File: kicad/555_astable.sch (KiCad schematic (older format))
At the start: 10 parts, among them U2 555

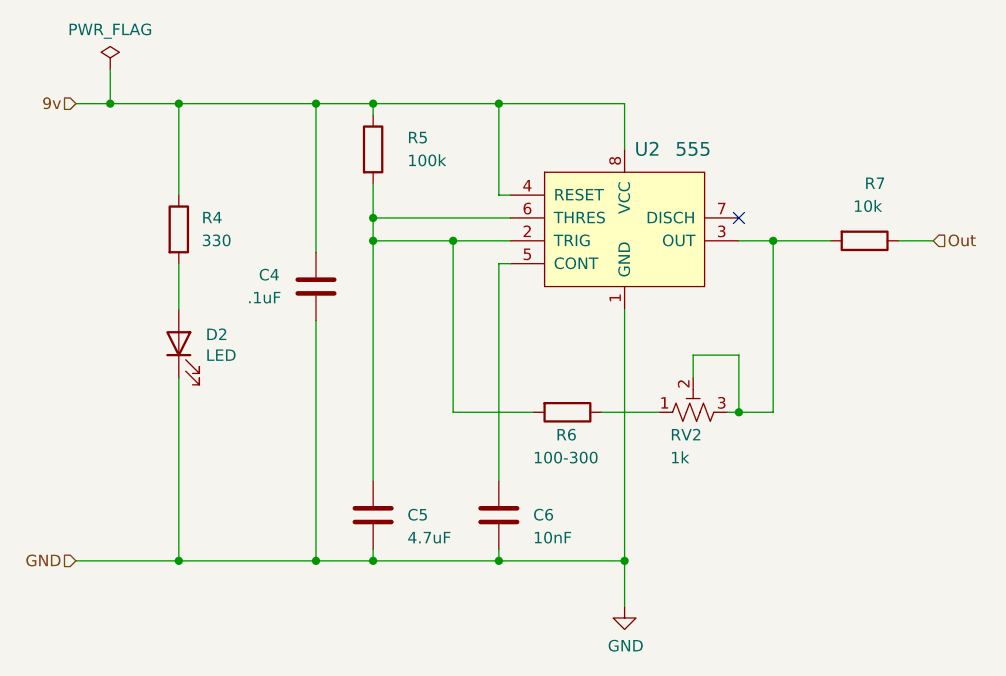
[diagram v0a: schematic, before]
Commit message: PCB revisions:
* Add voltage regulator to POLY_555
* Ditch hitch
* Reorder switches+circuits left to right
* Carve out room for battery
* Mark # 555s
* Label wired pins better

APC updates:

* Fix ground error
* Reverse volume pot direction
* Swap timing cap footprint
* Add stress relief hole for battery wires
* Widen speaker pins
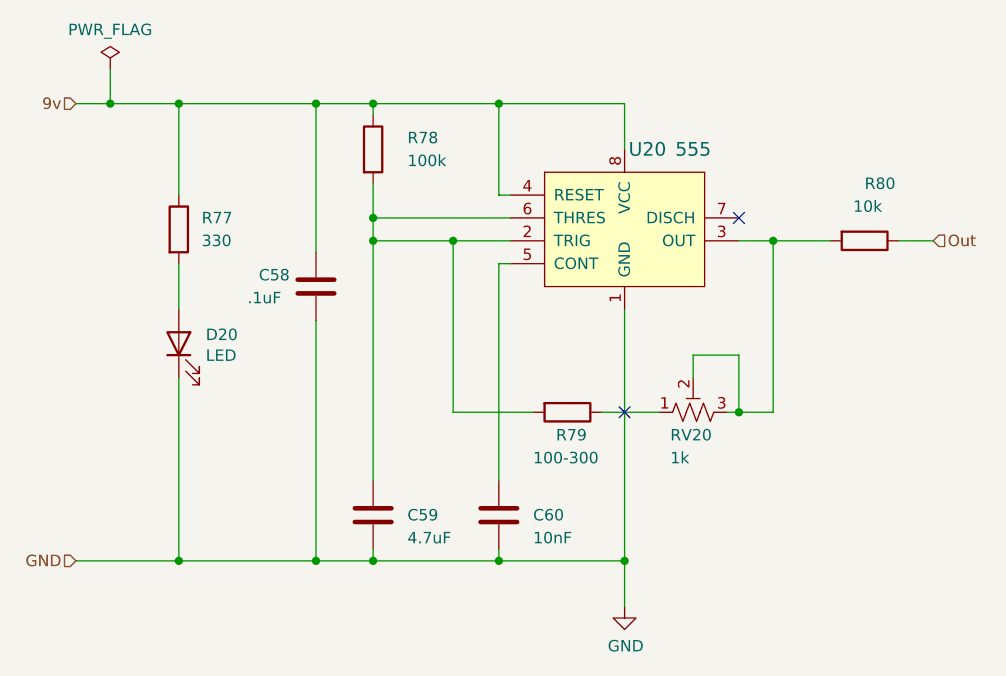
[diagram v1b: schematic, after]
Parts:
- renumbered C4 to C1, C5 to C2, C6 to C3, D2 to D1, R4 to R1, R5 to R2, R6 to R3, R7 to R4, RV2 to RV1, U2 to U1
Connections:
- no-connect marks 1 -> 2

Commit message: Update PCB
* Fix and expand battery cavity
* Fix S13-S20,C61,U21 label placements
* Fix uneven breakaway wall near APC
* Swap misplaced C62,R83 labels
* Assign C103 value
* Swap 4.7uF cap footprints and re-route
* Move LED
* Upgrade APC pots
* Move to 0,0
* Expand battery cavity even more
* Update branding: ditch _ and space, add rev, add to back side too
* Add APC rev too
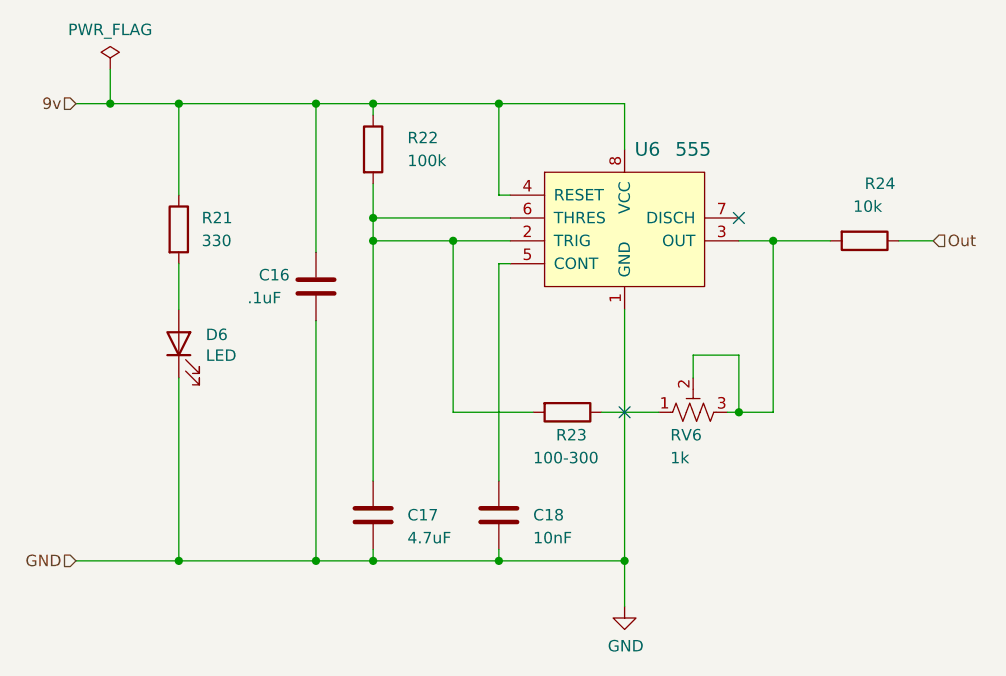
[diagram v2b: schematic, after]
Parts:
- C2: footprint Capacitor_THT:CP_Radial_D4.0mm_P2.00mm -> Capacitor_THT:CP_Radial_D5.0mm_P2.00mm
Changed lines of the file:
@@
 $Descr A4 11693 8268
 encoding utf-8
-Sheet 21 22
+Sheet 7 22
 Title ""
 Date ""
@@
 AR Path="/5F842C45/60F6A68E" Ref="R74"  Part="1"
 AR Path="/5F842C61/60F6A68E" Ref="R78"  Part="1"
-F 0 "R78" H 4750 3500 50  0000 L CNN
+F 0 "R22" H 4750 3500 50  0000 L CNN
 F 1 "100k" H 4750 3400 50  0000 L CNN
 F 2 "Resistor_THT:R_Axial_DIN0207_L6.3mm_D2.5mm_P2.54mm_Vertical" V 4530 3450 50  0001 C CNN
@@
 AR Path="/5F842C45/60F6EAC0" Ref="C55"  Part="1"
 AR Path="/5F842C61/60F6EAC0" Ref="C58"  Part="1"
-F 0 "C58" H 4100 4100 50  0000 L CNN
+F 0 "C16" H 4100 4100 50  0000 L CNN
 F 1 ".1uF" H 4050 4000 50  0000 L CNN
 F 2 "Capacitor_THT:C_Disc_D5.0mm_W2.5mm_P5.00mm" H 4388 3900 50  0001 C CNN
@@
 AR Path="/5F842C45/60F6A6DA" Ref="U19"  Part="1"
 AR Path="/5F842C61/60F6A6DA" Ref="U20"  Part="1"
-F 0 "U20" H 5800 4050 60  0000 C CNN
+F 0 "U6" H 5800 4050 60  0000 C CNN
 F 1 "555" H 6000 4050 60  0000 C CNN
 F 2 "Package_DIP:DIP-8_W7.62mm" H 5900 3950 60  0001 L CNN
@@
 AR Path="/5F842C45/60F6A6C5" Ref="RV19"  Part="1"
 AR Path="/5F842C61/60F6A6C5" Ref="RV20"  Part="1"
-F 0 "RV20" V 5900 4700 50  0000 R CNN
+F 0 "RV6" V 5900 4700 50  0000 R CNN
 F 1 "1k" V 5800 4700 50  0000 R CNN
 F 2 "Potentiometer_THT:Potentiometer_Piher_PT-6-V_Vertical" H 6000 4600 50  0001 C CNN
@@
 AR Path="/5F842C45/5EFAE830" Ref="R76"  Part="1"
 AR Path="/5F842C61/5EFAE830" Ref="R80"  Part="1"
-F 0 "R80" V 6500 3850 50  0000 L CNN
+F 0 "R24" V 6500 3850 50  0000 L CNN
 F 1 "10k" V 6600 3800 50  0000 L CNN
 F 2 "Resistor_THT:R_Axial_DIN0207_L6.3mm_D2.5mm_P2.54mm_Vertical" V 6680 3850 50  0001 C CNN
@@
 AR Path="/5F842C45/5F127BEF" Ref="D19"  Part="1"
 AR Path="/5F842C61/5F127BEF" Ref="D20"  Part="1"
-F 0 "D20" V 3789 4182 50  0000 R CNN
+F 0 "D6" V 3789 4182 50  0000 R CNN
 F 1 "LED" V 3698 4182 50  0000 R CNN
 F 2 "LED_THT:LED_D5.0mm" H 3750 4300 50  0001 C CNN
@@
 AR Path="/5F842C45/5F127BF5" Ref="R73"  Part="1"
 AR Path="/5F842C61/5F127BF5" Ref="R77"  Part="1"
-F 0 "R77" H 3850 3850 50  0000 L CNN
+F 0 "R21" H 3850 3850 50  0000 L CNN
 F 1 "330" H 3850 3750 50  0000 L CNN
 F 2 "Resistor_THT:R_Axial_DIN0207_L6.3mm_D2.5mm_P2.54mm_Vertical" V 3680 3800 50  0001 C CNN
@@
 AR Path="/5F842C45/60F6A6A0" Ref="C57"  Part="1"
 AR Path="/5F842C61/60F6A6A0" Ref="C60"  Part="1"
-F 0 "C60" H 5300 5050 50  0000 L CNN
+F 0 "C18" H 5300 5050 50  0000 L CNN
 F 1 "10nF" H 5300 4950 50  0000 L CNN
 F 2 "Capacitor_THT:C_Disc_D5.0mm_W2.5mm_P5.00mm" H 5188 4900 50  0001 C CNN
@@
 AR Path="/5F842C45/60F6A69A" Ref="C56"  Part="1"
 AR Path="/5F842C61/60F6A69A" Ref="C59"  Part="1"
-F 0 "C59" H 4750 5050 50  0000 L CNN
+F 0 "C17" H 4750 5050 50  0000 L CNN
 F 1 "4.7uF" H 4750 4950 50  0000 L CNN
-F 2 "Capacitor_THT:CP_Radial_D4.0mm_P2.00mm" H 4638 4900 50  0001 C CNN
+F 2 "Capacitor_THT:CP_Radial_D5.0mm_P2.00mm" H 4638 4900 50  0001 C CNN
 F 3 "~" H 4600 5050 50  0001 C CNN
 F 4 "Timing" H 4600 5050 50  0001 C CNN "Description"
@@
 AR Path="/5F842C45/5F3F39A8" Ref="R75"  Part="1"
 AR Path="/5F842C61/5F3F39A8" Ref="R79"  Part="1"
-F 0 "R79" V 5550 4550 50  0000 L CNN
+F 0 "R23" V 5550 4550 50  0000 L CNN
 F 1 "100-300" V 5650 4450 50  0000 L CNN
 F 2 "Resistor_THT:R_Axial_DIN0207_L6.3mm_D2.5mm_P2.54mm_Vertical" V 5380 4600 50  0001 C CNN
